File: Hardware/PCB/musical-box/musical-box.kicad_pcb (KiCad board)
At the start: 4 copper layers, 70 x 60 mm, 184 parts, among them J1 power, J201 PSU, J202 Jack-DC, J203 Li Ion 2S, J401 SPI Display, J402 Rotary Encoder 1, J403 I2C Display, J404 Rotary Encoder 2, J405 WS2812, J501 spk_out, J502 aux in, J503 line in, P201 USB_C, P202 ICT-Point, P203 ICT-Point, P204 ICT-Point, Q201 DMP3017SFK, Q204 IRF9362, Q301 BC846BDW1, SW301 boot, SW302 reset, U201 STUSB4500QTR, U202 MP2615, U203 TPS56339, U204 TLV75733PDBV, U205 TLV75733PDBV, U206 TLV803EC30DBZR, U301 CH340C, U302 ESP32-WROVER, U401 PCF8574ATS, U501 SPH0644HM4H-1, U502 SPH0644HM4H-1, U503 TAS5754MDCA

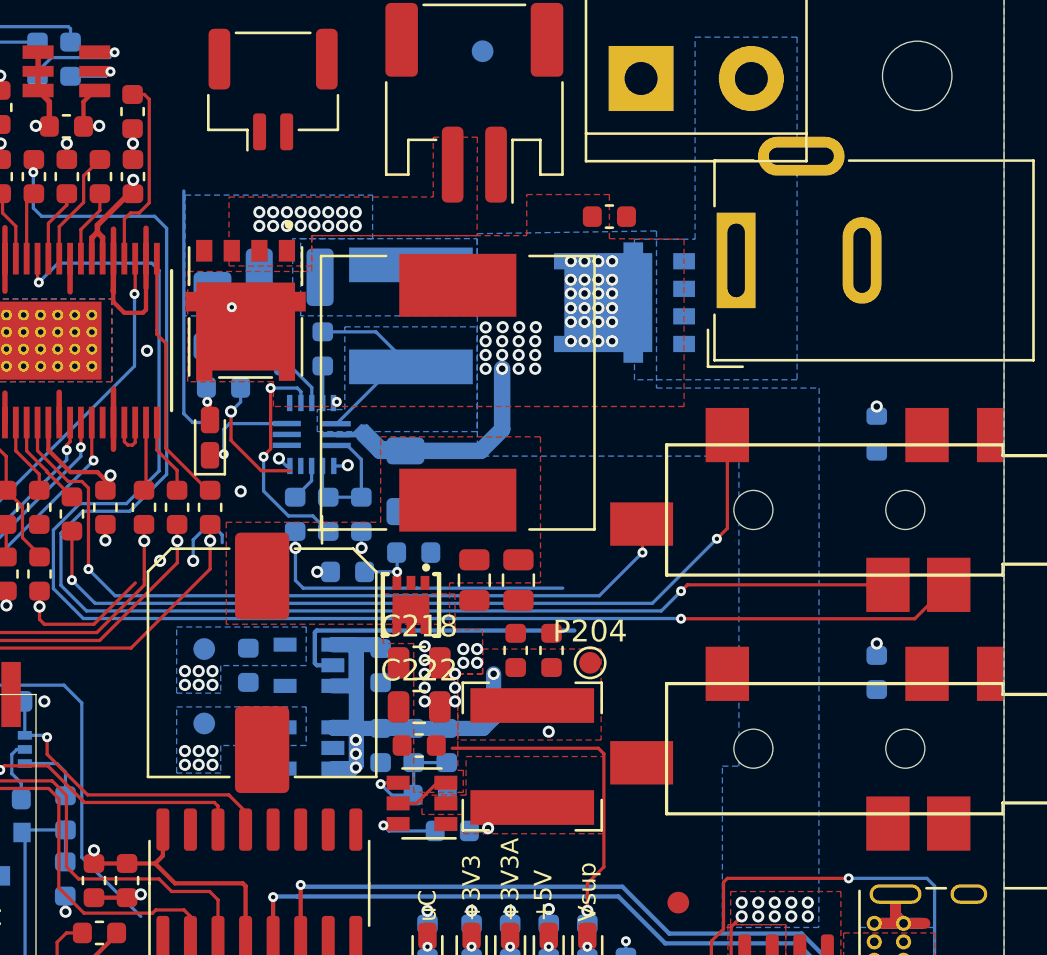
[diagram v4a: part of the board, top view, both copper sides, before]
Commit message: Fix battery charger circuit
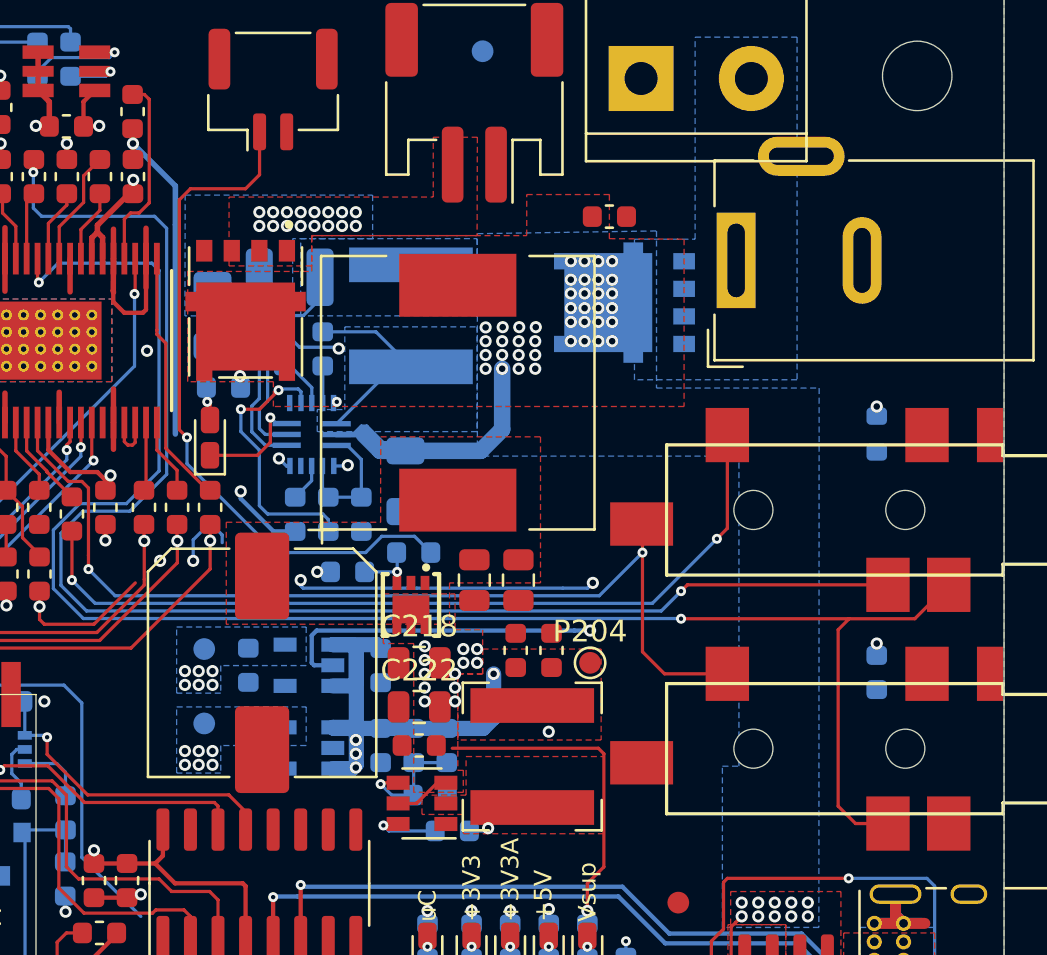
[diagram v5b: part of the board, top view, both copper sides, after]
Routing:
- net Net-(J1-Pad1): track 0.00 -> 32.0 mm, vias 0 -> 1
- net /Audio Output/DAC_OUTB: track 67.6 -> 79.1 mm
- net Net-(L202-Pad2): track 0.00 -> 10.3 mm
- net /Audio Output/DAC_OUTA: track 36.3 -> 45.2 mm
- net GND: track 156.5 -> 164.5 mm, vias 61 -> 63
- net VDC: track 29.7 -> 24.3 mm
- net Net-(C212-Pad2): track 4.59 -> 9.25 mm, vias 17 -> 16
- net Net-(R215-Pad2): track 10.7 -> 12.5 mm

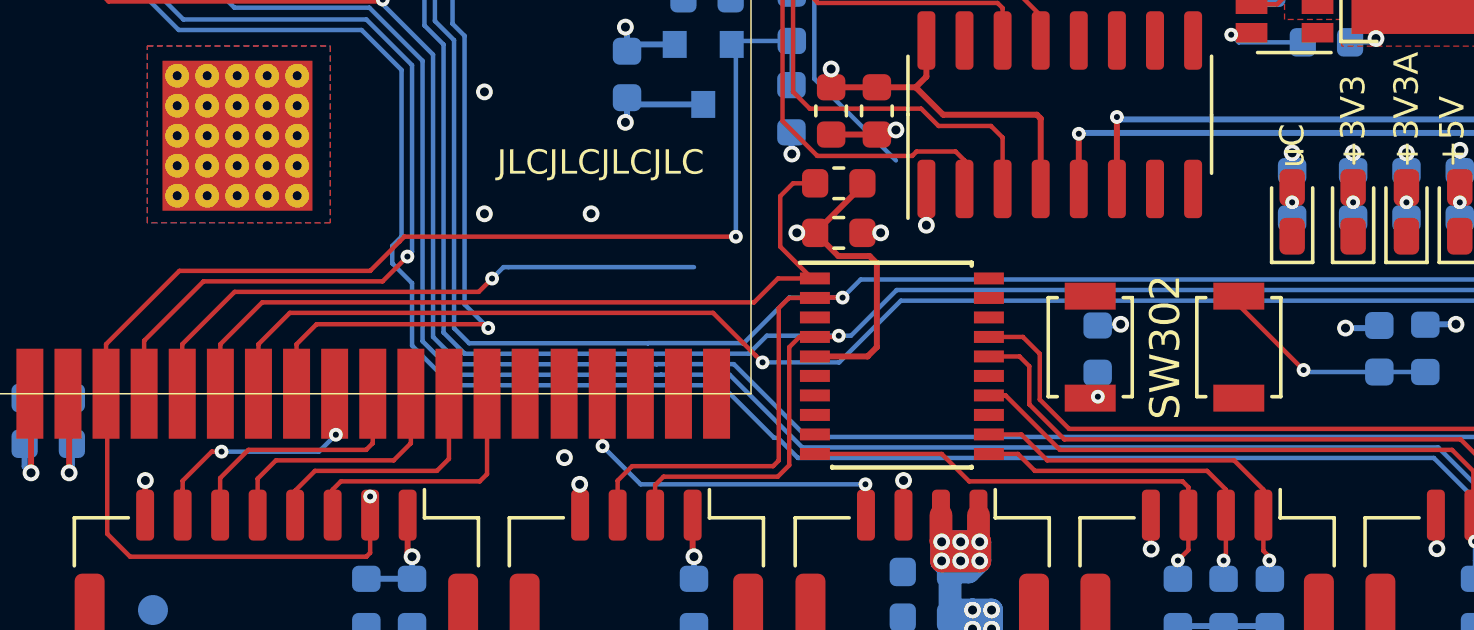
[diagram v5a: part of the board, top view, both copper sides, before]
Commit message: Swap aux and line detect for better routing
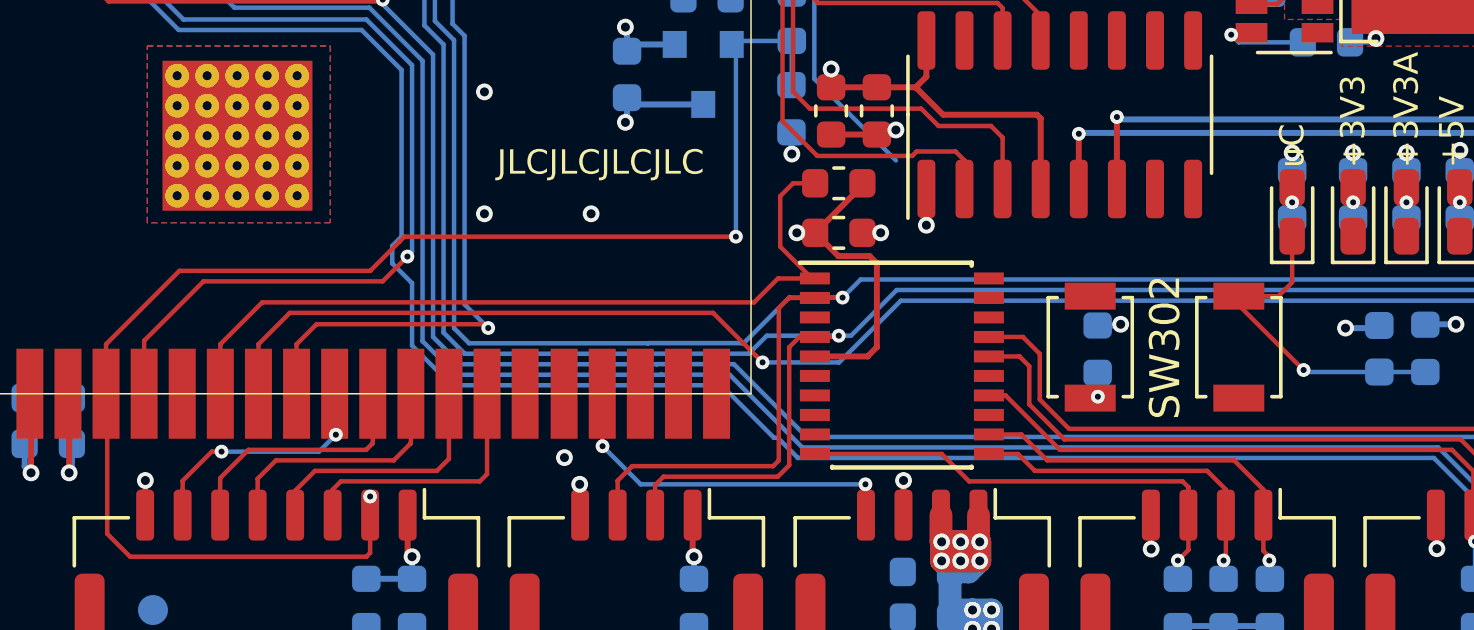
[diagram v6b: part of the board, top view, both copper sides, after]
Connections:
- J503 pad S: /Microcontroller/I39 -> /Microcontroller/IO12
- R509 pad 1: /Microcontroller/I39 -> /Microcontroller/IO12
- U302 pad 14: /Audio Output/AUX_Detect -> /Microcontroller/IO12
- U302 pad 5: /Microcontroller/I39 -> /Audio Output/AUX_Detect
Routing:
- net /Microcontroller/I39: track 19.8 -> 0.00 mm, vias 1 -> 0
- net /Microcontroller/IO00: track 29.0 -> 32.5 mm
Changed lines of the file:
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@@
     (thickness 1.6)
     (drawings 12)
-    (tracks 1661)
+    (tracks 1656)
     (zones 0)
     (modules 184)
@@
   (net 147 "/Audio Output/SPK_INB")
   (net 148 "/Audio Output/AUX_Detect")
-  (net 149 /Microcontroller/I39)
-  (net 150 "Net-(J1-Pad1)")
+  (net 149 "Net-(J1-Pad1)")
+  (net 150 /Microcontroller/IO12)
   (net_class Default "This is the default net class."
     (clearance 0.2)
@@
     (add_net /Microcontroller/I35)
     (add_net /Microcontroller/I36)
-    (add_net /Microcontroller/I39)
     (add_net /Microcontroller/IO00)
     (add_net /Microcontroller/IO02)
     (add_net /Microcontroller/IO04)
     (add_net /Microcontroller/IO05)
+    (add_net /Microcontroller/IO12)
     (add_net /Microcontroller/IO13)
     (add_net /Microcontroller/IO14)
@@
       (net 1 GND))
     (pad S smd rect (at 0.6 3.45 180) (size 1.2 2.5) (layers F.Cu F.Paste F.Mask)
-      (net 149 /Microcontroller/I39))
+      (net 150 /Microcontroller/IO12))
   )
   (module SilentWorks:PJ328B (layer F.Cu)
@@
       (net 1 GND))
     (pad 1 smd roundrect (at -0.625 1.95) (size 0.6 1.7) (layers F.Cu F.Paste F.Mask) (roundrect_rratio 0.25)
-      (net 150 "Net-(J1-Pad1)"))
+      (net 149 "Net-(J1-Pad1)"))
     (model ${KISYS3DMOD}/Connector_JST.3dshapes/JST_GH_BM02B-GHS-TBT_1x02-1MP_P1.25mm_Vertical.wrl
       (at (xyz 0 0 0))
@@
       (net 93 /Microcontroller/I36))
     (pad 5 smd rect (at -9 5.99 90) (size 3 0.9) (layers F.Cu F.Paste F.Mask)
-      (net 149 /Microcontroller/I39))
+      (net 148 "/Audio Output/AUX_Detect"))
     (pad 6 smd rect (at -9 7.26 90) (size 3 0.9) (layers F.Cu F.Paste F.Mask)
       (net 94 /Microcontroller/I34))
@@
       (net 25 /Microcontroller/IO14))
     (pad 14 smd rect (at -9 17.42 90) (size 3 0.9) (layers F.Cu F.Paste F.Mask)
-      (net 148 "/Audio Output/AUX_Detect"))
+      (net 150 /Microcontroller/IO12))
     (pad 15 smd rect (at -9 18.72 90) (size 3 0.9) (layers F.Cu F.Paste F.Mask)
       (net 1 GND))
@@
       (net 3 +3V3))
     (pad 1 smd roundrect (at -0.7875 0 90) (size 0.875 0.95) (layers B.Cu B.Paste B.Mask) (roundrect_rratio 0.25)
-      (net 149 /Microcontroller/I39))
+      (net 150 /Microcontroller/IO12))
     (model ${KISYS3DMOD}/Resistor_SMD.3dshapes/R_0603_1608Metric.wrl
       (at (xyz 0 0 0))
@@
       (net 75 "Net-(Q201-Pad3)"))
     (pad 1 smd roundrect (at -0.7875 0 180) (size 0.875 0.95) (layers B.Cu B.Paste B.Mask) (roundrect_rratio 0.25)
-      (net 150 "Net-(J1-Pad1)"))
+      (net 149 "Net-(J1-Pad1)"))
     (model ${KISYS3DMOD}/Resistor_SMD.3dshapes/R_0603_1608Metric.wrl
       (at (xyz 0 0 0))
@@
   (segment (start 391.656 172.554) (end 391.656 172.251) (width 0.15) (layer F.Cu) (net 5))
   (segment (start 393.815 174.713) (end 391.656 172.554) (width 0.15) (layer F.Cu) (net 5))
+  (segment (start 391.656 172.251) (end 392.975 172.251) (width 0.15) (layer F.Cu) (net 5))
+  (segment (start 393.434 171.792) (end 393.434 170.255) (width 0.15) (layer F.Cu) (net 5))
+  (segment (start 392.975 172.251) (end 393.434 171.792) (width 0.15) (layer F.Cu) (net 5))
   (segment (start 383.42 149.6675) (end 383.42 150.417) (width 0.15) (layer F.Cu) (net 6))
   (via (at 383.42 150.417) (size 0.56) (drill 0.3) (layers F.Cu B.Cu) (net 6))
@@
   (segment (start 375.273 135.089) (end 375.654 135.47) (width 0.15) (layer B.Cu) (net 147))
   (segment (start 375.273 133.438) (end 375.273 135.089) (width 0.15) (layer B.Cu) (net 147))
-  (via (at 366.764 171.665) (size 0.46) (drill 0.2) (layers F.Cu B.Cu) (net 149))
-  (segment (start 358.18302 172.10798) (end 366.32102 172.10798) (width 0.15) (layer F.Cu) (net 149))
-  (segment (start 367.145 171.284) (end 366.764 171.665) (width 0.15) (layer B.Cu) (net 149))
-  (segment (start 373.495 171.284) (end 367.309894 171.284) (width 0.15) (layer B.Cu) (net 149))
-  (segment (start 367.309894 171.284) (end 367.145 171.284) (width 0.15) (layer B.Cu) (net 149))
-  (segment (start 356.437 173.854) (end 358.18302 172.10798) (width 0.15) (layer F.Cu) (net 149))
-  (segment (start 356.437 175.504) (end 356.437 173.854) (width 0.15) (layer F.Cu) (net 149))
-  (segment (start 366.32102 172.10798) (end 366.764 171.665) (width 0.15) (layer F.Cu) (net 149))
-  (segment (start 385.697 131.578) (end 385.697 133.555) (width 0.15) (layer F.Cu) (net 150))
-  (segment (start 385.697 133.555) (end 385.052 134.2) (width 0.15) (layer F.Cu) (net 150))
-  (segment (start 385.052 134.2) (end 382.512 134.2) (width 0.15) (layer F.Cu) (net 150))
-  (segment (start 382.001999 134.710001) (end 382.001999 140.674999) (width 0.15) (layer F.Cu) (net 150))
-  (segment (start 382.512 134.2) (end 382.001999 134.710001) (width 0.15) (layer F.Cu) (net 150))
-  (via (at 382.353174 145.657472) (size 0.46) (drill 0.2) (layers F.Cu B.Cu) (net 150))
-  (segment (start 382.001999 145.306297) (end 382.353174 145.657472) (width 0.15) (layer F.Cu) (net 150))
-  (segment (start 382.001999 140.674999) (end 382.001999 145.306297) (width 0.15) (layer F.Cu) (net 150))
-  (segment (start 382.353174 145.657472) (end 382.353174 146.868174) (width 0.15) (layer B.Cu) (net 150))
-  (segment (start 391.332794 150.21399) (end 390.582784 150.964) (width 0.15) (layer B.Cu) (net 150))
-  (segment (start 392.83649 150.21399) (end 391.332794 150.21399) (width 0.15) (layer B.Cu) (net 150))
-  (segment (start 393.5865 150.964) (end 392.83649 150.21399) (width 0.15) (layer B.Cu) (net 150))
-  (segment (start 390.582784 150.964) (end 386.449 150.964) (width 0.15) (layer B.Cu) (net 150))
-  (segment (start 382.353174 146.868174) (end 386.449 150.964) (width 0.15) (layer B.Cu) (net 150))
+  (segment (start 385.697 131.578) (end 385.697 133.555) (width 0.15) (layer F.Cu) (net 149))
+  (segment (start 385.697 133.555) (end 385.052 134.2) (width 0.15) (layer F.Cu) (net 149))
+  (segment (start 385.052 134.2) (end 382.512 134.2) (width 0.15) (layer F.Cu) (net 149))
+  (segment (start 382.001999 134.710001) (end 382.001999 140.674999) (width 0.15) (layer F.Cu) (net 149))
+  (segment (start 382.512 134.2) (end 382.001999 134.710001) (width 0.15) (layer F.Cu) (net 149))
+  (via (at 382.353174 145.657472) (size 0.46) (drill 0.2) (layers F.Cu B.Cu) (net 149))
+  (segment (start 382.001999 145.306297) (end 382.353174 145.657472) (width 0.15) (layer F.Cu) (net 149))
+  (segment (start 382.001999 140.674999) (end 382.001999 145.306297) (width 0.15) (layer F.Cu) (net 149))
+  (segment (start 382.353174 145.657472) (end 382.353174 146.868174) (width 0.15) (layer B.Cu) (net 149))
+  (segment (start 391.332794 150.21399) (end 390.582784 150.964) (width 0.15) (layer B.Cu) (net 149))
+  (segment (start 392.83649 150.21399) (end 391.332794 150.21399) (width 0.15) (layer B.Cu) (net 149))
+  (segment (start 393.5865 150.964) (end 392.83649 150.21399) (width 0.15) (layer B.Cu) (net 149))
+  (segment (start 390.582784 150.964) (end 386.449 150.964) (width 0.15) (layer B.Cu) (net 149))
+  (segment (start 382.353174 146.868174) (end 386.449 150.964) (width 0.15) (layer B.Cu) (net 149))
   (zone (net 1) (net_name GND) (layer In2.Cu) (hatch edge 0.508)
     (connect_pads thru_hole_only (clearance 0.2))
